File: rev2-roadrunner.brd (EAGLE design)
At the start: 49.5 x 34.3 mm, 26 parts, among them J1 USB_MINI-B_SMT, Y1 16MHz

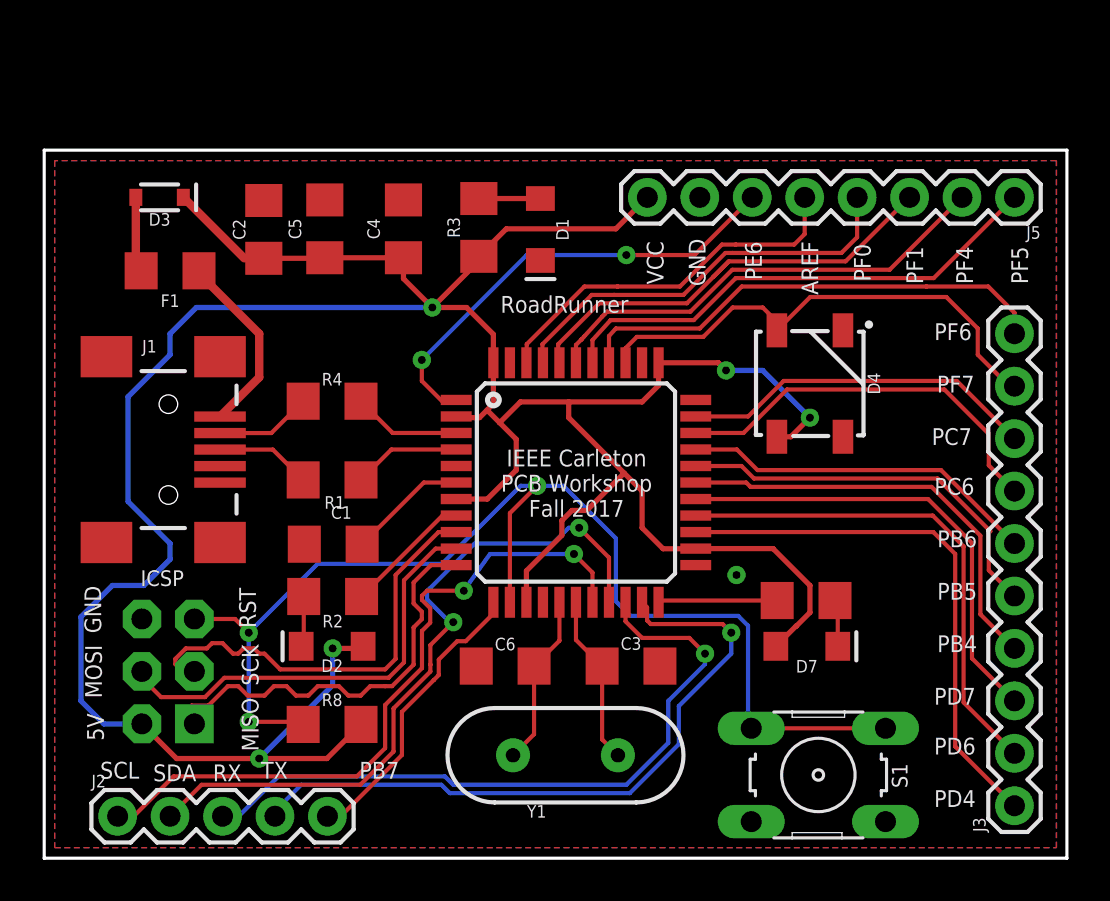
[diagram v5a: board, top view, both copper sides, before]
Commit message: Added Icons and redid routing
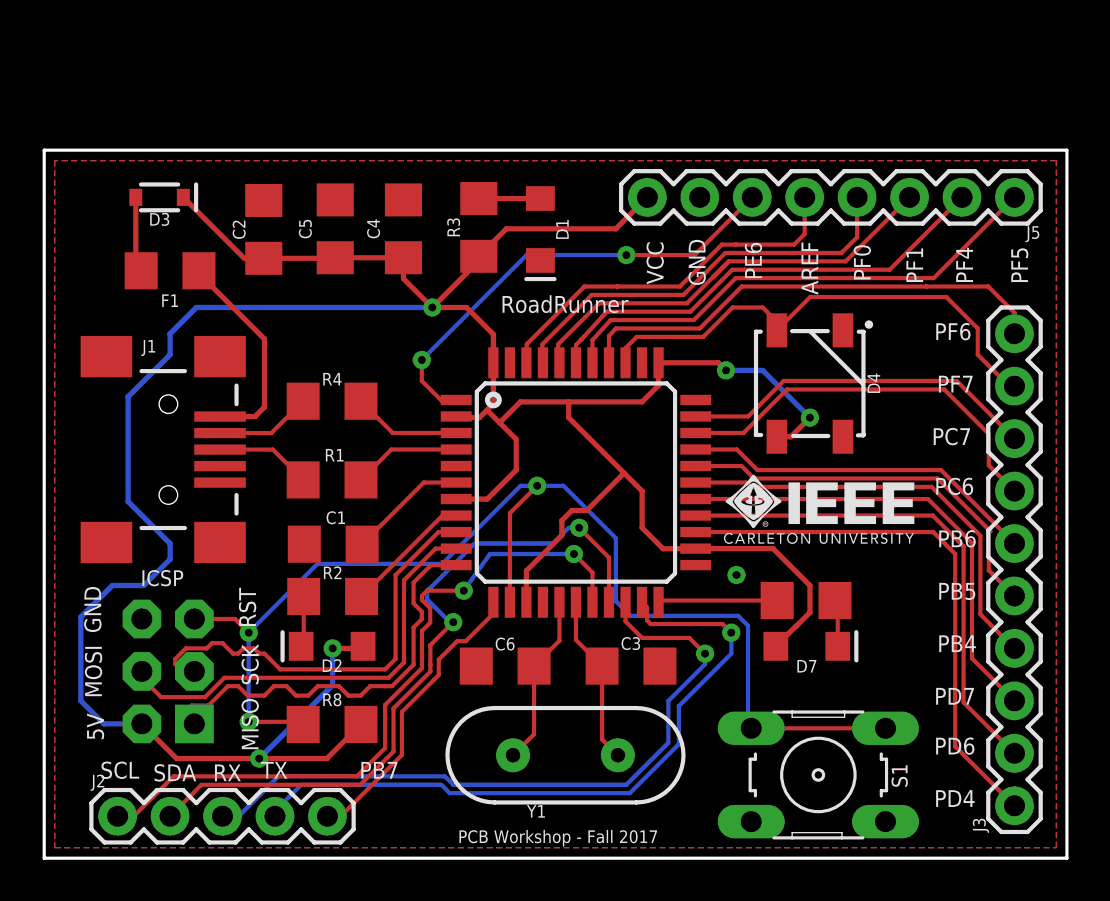
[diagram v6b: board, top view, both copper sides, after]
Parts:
- added U$2: (no value), ieeeCarletonLogo:IEEECARLETON-ROADRUNNER
- moved C5 0.51 mm to (14.1, 30.5)
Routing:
- net USB_VCC: track 9.05 -> 10.3 mm
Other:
- board text added: "PCB Workshop - Fall 2017"
- board text removed: "IEEE Carleton PCB Workshop Fall 2017"
